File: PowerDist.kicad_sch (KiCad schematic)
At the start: 13 parts, among them J7 PowerConn, U2 RI3-1205S, U3 NCP1117-3.3_SOT223

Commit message: bom, gerbers, edge cuts, footprint verification
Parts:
- C21: P/N (none) -> 22201C106KAT2A
- C22, C23: P/N (none) -> 0805YC106KAT2A
- J7: P/N (none) -> 43650-0227
- R5: P/N (none) -> CRCW080521K5FKEA
- TP1, TP2, TP3, TP4, TP5: P/N (none) -> 5005
- U2: P/N (none) -> RI3-1205S
- U3: value NCP1117-3.3_SOT223 -> LD1117-3.3_SOT223; P/N (none) -> LD1117S33TR
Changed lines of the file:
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@@
       (effects (font (size 1.27 1.27)) hide)
     )
-    (property "Datasheet" "~" (at 92.71 86.36 0)
+    (property "Datasheet" "https://www.mouser.com/datasheet/2/40/X7RDielectric-2943470.pdf" (at 92.71 86.36 0)
+      (effects (font (size 1.27 1.27)) hide)
+    )
+    (property "P/N" "22201C106KAT2A" (at 92.71 86.36 0)
       (effects (font (size 1.27 1.27)) hide)
     )
@@
       (effects (font (size 1.27 1.27)) hide)
     )
-    (property "Datasheet" "~" (at 87.63 80.01 0)
+    (property "Datasheet" "https://www.mouser.com/datasheet/2/215/5005_5009-741322.pdf" (at 87.63 80.01 0)
+      (effects (font (size 1.27 1.27)) hide)
+    )
+    (property "P/N" "5005" (at 82.55 80.01 0)
       (effects (font (size 1.27 1.27)) hide)
     )
@@
       (effects (font (size 1.27 1.27)) hide)
     )
-    (property "Datasheet" "~" (at 143.51 80.01 0)
+    (property "Datasheet" "https://www.mouser.com/datasheet/2/215/5005_5009-741322.pdf" (at 143.51 80.01 0)
+      (effects (font (size 1.27 1.27)) hide)
+    )
+    (property "P/N" "5005" (at 138.43 80.01 0)
       (effects (font (size 1.27 1.27)) hide)
     )
@@
       (effects (font (size 1.27 1.27)) hide)
     )
-    (property "Datasheet" "~" (at 133.35 93.98 0)
+    (property "Datasheet" "https://www.mouser.com/datasheet/2/215/5005_5009-741322.pdf" (at 133.35 93.98 0)
+      (effects (font (size 1.27 1.27)) hide)
+    )
+    (property "P/N" "5005" (at 138.43 93.98 0)
       (effects (font (size 1.27 1.27)) hide)
     )
@@
     )
     (property "Datasheet" "https://www.mouser.com/datasheet/2/468/RI3-1711119.pdf" (at 114.3 81.28 0)
+      (effects (font (size 1.27 1.27)) hide)
+    )
+    (property "P/N" "RI3-1205S" (at 114.3 81.28 0)
       (effects (font (size 1.27 1.27)) hide)
     )
@@
       (effects (font (size 1.27 1.27)) hide)
     )
-    (property "Datasheet" "~" (at 161.29 91.44 0)
+    (property "Datasheet" "https://www.mouser.com/datasheet/2/216/APTD2012LCGCK-1102037.pdf" (at 161.29 91.44 0)
       (effects (font (size 1.27 1.27)) hide)
     )
@@
       (effects (font (size 1.27 1.27)) hide)
     )
-    (property "Datasheet" "~" (at 161.29 82.55 0)
+    (property "Datasheet" "https://www.mouser.com/datasheet/2/427/dcrcwe3-1762152.pdf" (at 161.29 82.55 0)
+      (effects (font (size 1.27 1.27)) hide)
+    )
+    (property "P/N" "CRCW080521K5FKEA" (at 161.29 82.55 0)
       (effects (font (size 1.27 1.27)) hide)
     )
@@
       (effects (font (size 1.27 1.27)))
     )
-    (property "Value" "NCP1117-3.3_SOT223" (at 204.47 77.4446 0)
+    (property "Value" "LD1117-3.3_SOT223" (at 204.47 77.4446 0)
       (effects (font (size 1.27 1.27)))
     )
@@
       (effects (font (size 1.27 1.27)) hide)
     )
-    (property "Datasheet" "http://www.st.com/st-web-ui/static/active/en/resource/technical/document/datasheet/CD00000544.pdf" (at 207.01 87.63 0)
+    (property "Datasheet" "https://www.mouser.com/datasheet/2/389/ld1117-1849389.pdf" (at 207.01 87.63 0)
+      (effects (font (size 1.27 1.27)) hide)
+    )
+    (property "P/N" "LD1117S33TR" (at 204.47 81.28 0)
       (effects (font (size 1.27 1.27)) hide)
     )
@@
       (effects (font (size 1.27 1.27)) hide)
     )
-    (property "Datasheet" "~" (at 191.77 86.36 0)
+    (property "Datasheet" "https://www.mouser.com/datasheet/2/40/AVX_X7RDielectric_777024-1853642.pdf" (at 191.77 86.36 0)
+      (effects (font (size 1.27 1.27)) hide)
+    )
+    (property "P/N" "0805YC106KAT2A" (at 191.77 86.36 0)
       (effects (font (size 1.27 1.27)) hide)
     )
@@
       (effects (font (size 1.27 1.27)) hide)
     )
-    (property "Datasheet" "~" (at 217.17 86.36 0)
+    (property "Datasheet" "https://www.mouser.com/datasheet/2/40/AVX_X7RDielectric_777024-1853642.pdf" (at 217.17 86.36 0)
+      (effects (font (size 1.27 1.27)) hide)
+    )
+    (property "P/N" "0805YC106KAT2A" (at 217.17 86.36 0)
       (effects (font (size 1.27 1.27)) hide)
     )
@@
       (effects (font (size 1.27 1.27)) hide)
     )
-    (property "Datasheet" "~" (at 227.33 80.01 0)
+    (property "Datasheet" "https://www.mouser.com/datasheet/2/215/5005_5009-741322.pdf" (at 227.33 80.01 0)
+      (effects (font (size 1.27 1.27)) hide)
+    )
+    (property "P/N" "5005" (at 222.25 80.01 0)
       (effects (font (size 1.27 1.27)) hide)
     )
@@
       (effects (font (size 1.27 1.27)) hide)
     )
-    (property "Datasheet" "~" (at 77.47 92.71 0)
+    (property "Datasheet" "https://www.mouser.com/datasheet/2/215/5005_5009-741322.pdf" (at 77.47 92.71 0)
+      (effects (font (size 1.27 1.27)) hide)
+    )
+    (property "P/N" "5005" (at 82.55 92.71 0)
       (effects (font (size 1.27 1.27)) hide)
     )
@@
       (effects (font (size 1.27 1.27)) hide)
     )
-    (property "Datasheet" "~" (at 68.58 85.09 0)
-      (effects (font (size 1.27 1.27)) hide)
-    )
+    (property "Datasheet" "https://www.mouser.com/datasheet/2/276/0436500227_PCB_HEADERS-168471.pdf" (at 68.58 85.09 0)
+      (effects (font (size 1.27 1.27)) hide)
+    )
+    (property "P/N" "43650-0227" (at 68.58 85.09 0)
+      (effects (font (size 1.27 1.27)) hide)
+    )

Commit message: began input/breakout changes
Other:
- note added: "***add mosfet power protection!!!"
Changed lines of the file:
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@@
     (stroke (width 0) (type default))
+  )
+  (text "***add mosfet power protection!!!" (at 135.255 24.13 0)
+    (effects (font (size 1.27 1.27)) (justify left bottom))
   )
   (text "Power GND\n(External)" (at 99.06 59.69 0)

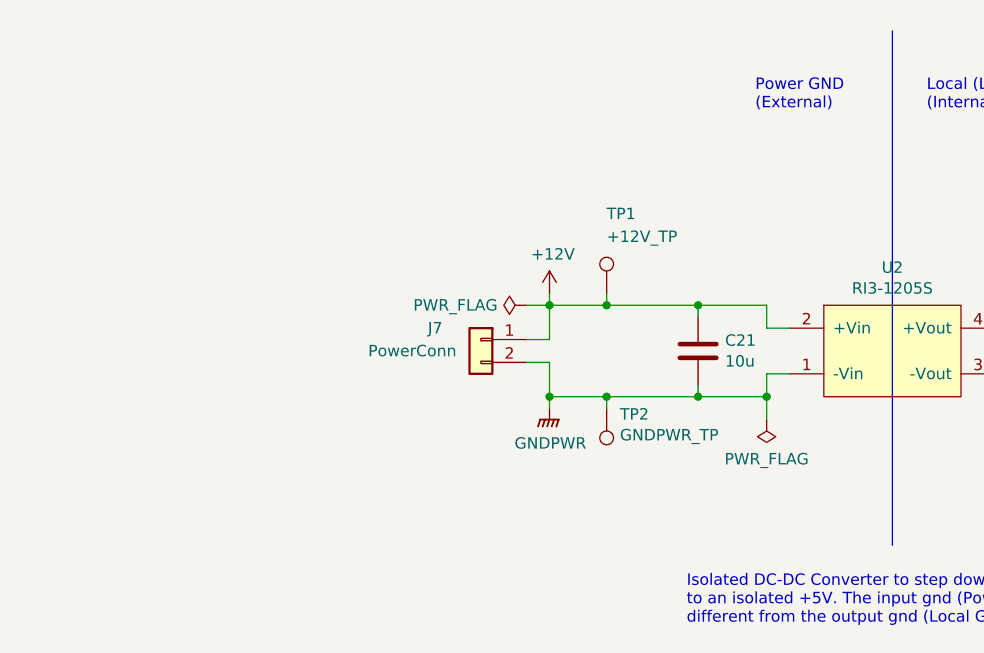
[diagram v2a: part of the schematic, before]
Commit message: new bt module + preliminary reverse protection
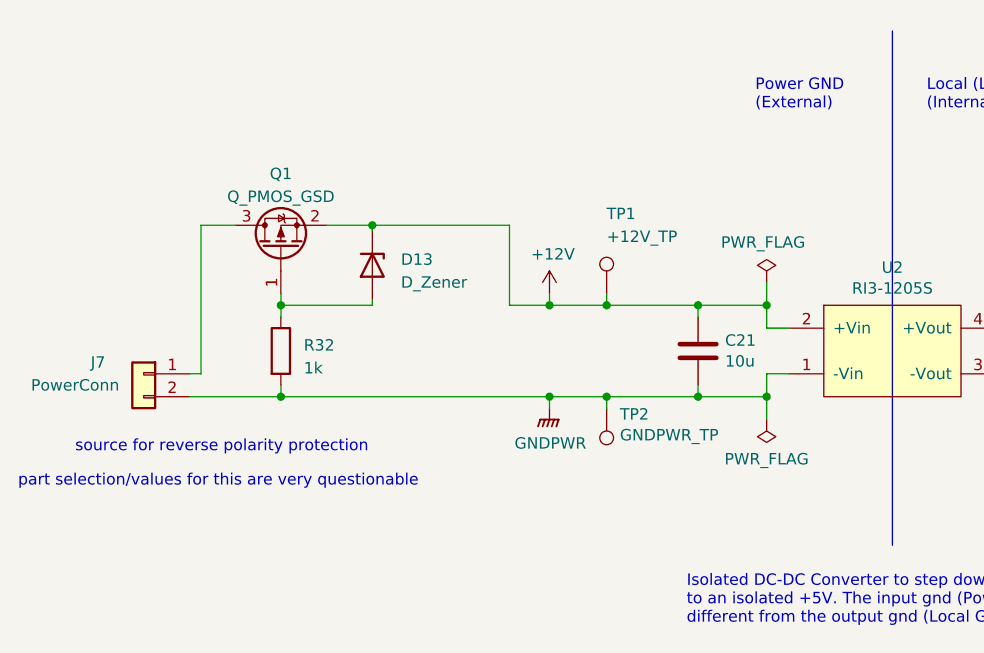
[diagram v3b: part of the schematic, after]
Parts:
- added D13: D_Zener, Diode_SMD:D_SOD-123F, symbol Device:D_Zener
- added Q1: Q_PMOS_GSD, Package_TO_SOT_SMD:SuperSOT-3, symbol Device:Q_PMOS_GSD
- added R32: 1k, Resistor_SMD:R_0805_2012Metric, symbol Device:R
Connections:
- net +12V: now also D13.1 (K), Q1.2 (S); no longer J7.1 (Pin_1)
- net GNDPWR: now also R32.2
- new net: J7.1 (Pin_1), Q1.3 (D)
- new net: D13.2 (A), Q1.1 (G), R32.1
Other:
- note added: "part selection/values for this are very questionable"
- note added: "source for reverse polarity protection"
- moved on the sheet: J7
